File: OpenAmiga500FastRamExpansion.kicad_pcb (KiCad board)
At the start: 2 copper layers, 100 x 71.5 mm, 35 parts, among them J1 68000_SOCKET, P1 JTAG_CONNECTOR, P99 OSHW_LOGO, U1 68000D, U2 74LS157, U3 74LS157, U4 ATF1502AS-10JU44, U5 HYB5118160BSJ, U6 HYB5118160BSJ, U7 HYB5118160BSJ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

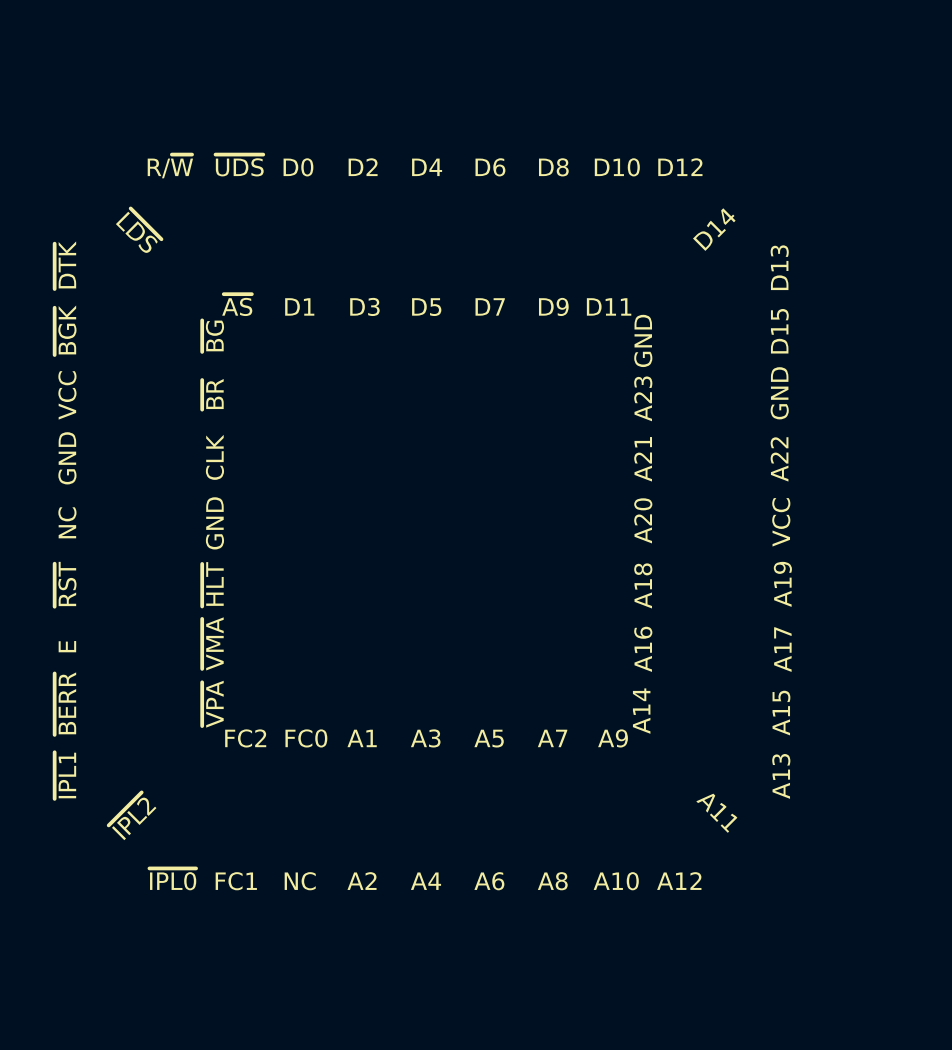
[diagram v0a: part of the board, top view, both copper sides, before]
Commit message: Remove old pin names
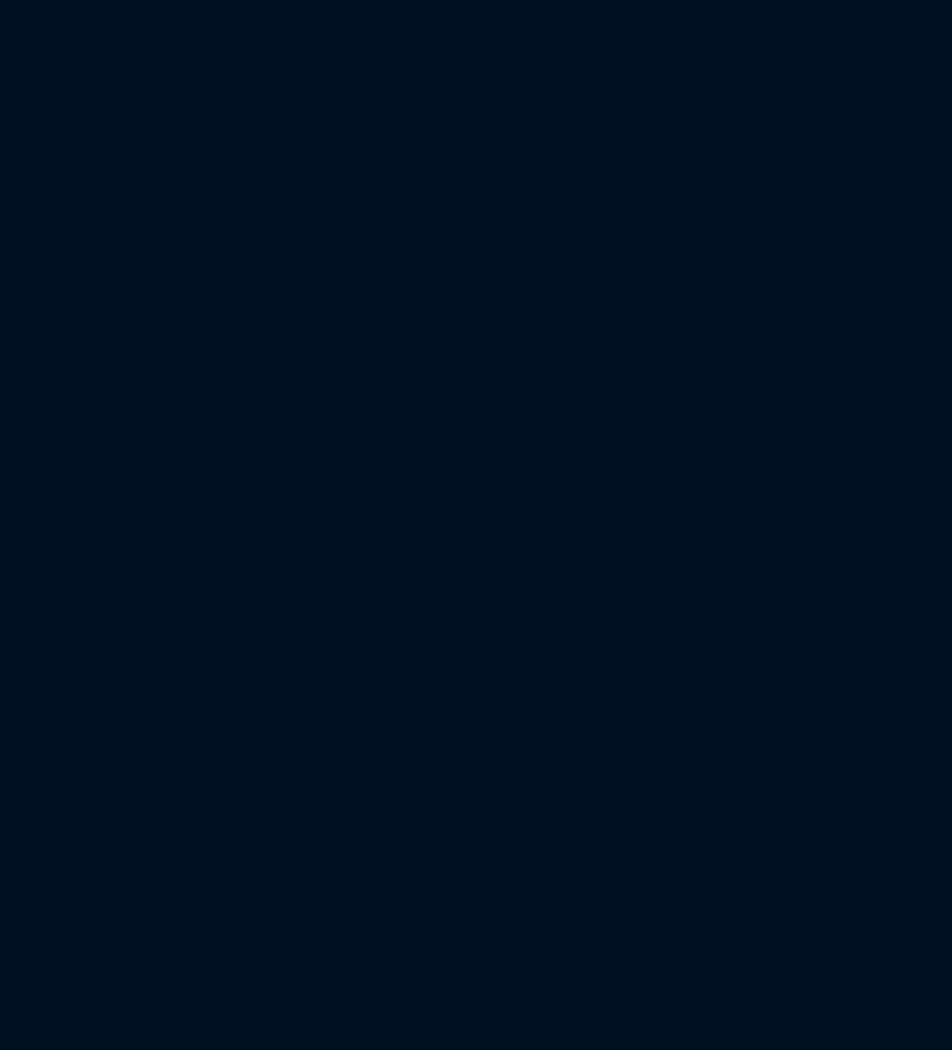
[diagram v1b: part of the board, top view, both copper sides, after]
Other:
- board text removed: "A1"
- board text removed: "A10"
- board text removed: "A11"
- board text removed: "A12"
- board text removed: "A13"
- board text removed: "A14"
- board text removed: "A15"
- board text removed: "A16"
- board text removed: "A17"
- board text removed: "A18"
- board text removed: "A19"
- board text removed: "A2"
- board text removed: "A20"
- board text removed: "A21"
- board text removed: "A22"
- board text removed: "A23"
- board text removed: "A3"
- board text removed: "A4"
- board text removed: "A5"
- board text removed: "A6"
- board text removed: "A7"
- board text removed: "A8"
- board text removed: "A9"
- board text removed: "CLK"
- board text removed: "D0"
- board text removed: "D1"
- board text removed: "D10"
- board text removed: "D11"
- board text removed: "D12"
- board text removed: "D13"
- board text removed: "D14"
- board text removed: "D15"
- board text removed: "D2"
- board text removed: "D3"
- board text removed: "D4"
- board text removed: "D5"
- board text removed: "D6"
- board text removed: "D7"
- board text removed: "D8"
- board text removed: "D9"
- board text removed: "E"
- board text removed: "FC0"
- board text removed: "FC1"
- board text removed: "FC2"
- board text removed: "NC"
- board text removed: "R/~W"
- board text removed: "~AS"
- board text removed: "~BERR"
- board text removed: "~BG"
- board text removed: "~BGK"
- board text removed: "~BR"
- board text removed: "~DTK"
- board text removed: "~HLT"
- board text removed: "~IPL0"
- board text removed: "~IPL1"
- board text removed: "~IPL2"
- board text removed: "~LDS"
- board text removed: "~RST"
- board text removed: "~UDS"
- board text removed: "~VMA"
- board text removed: "~VPA"
